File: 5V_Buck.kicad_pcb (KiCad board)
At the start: 2 copper layers, 34 x 40 mm, 12 parts, among them J1 POWER_JACK1, M1 USB+SHIELDUSB-A-S-NOSILK-FEMA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, U1 ADP2303ARDZ-5.0

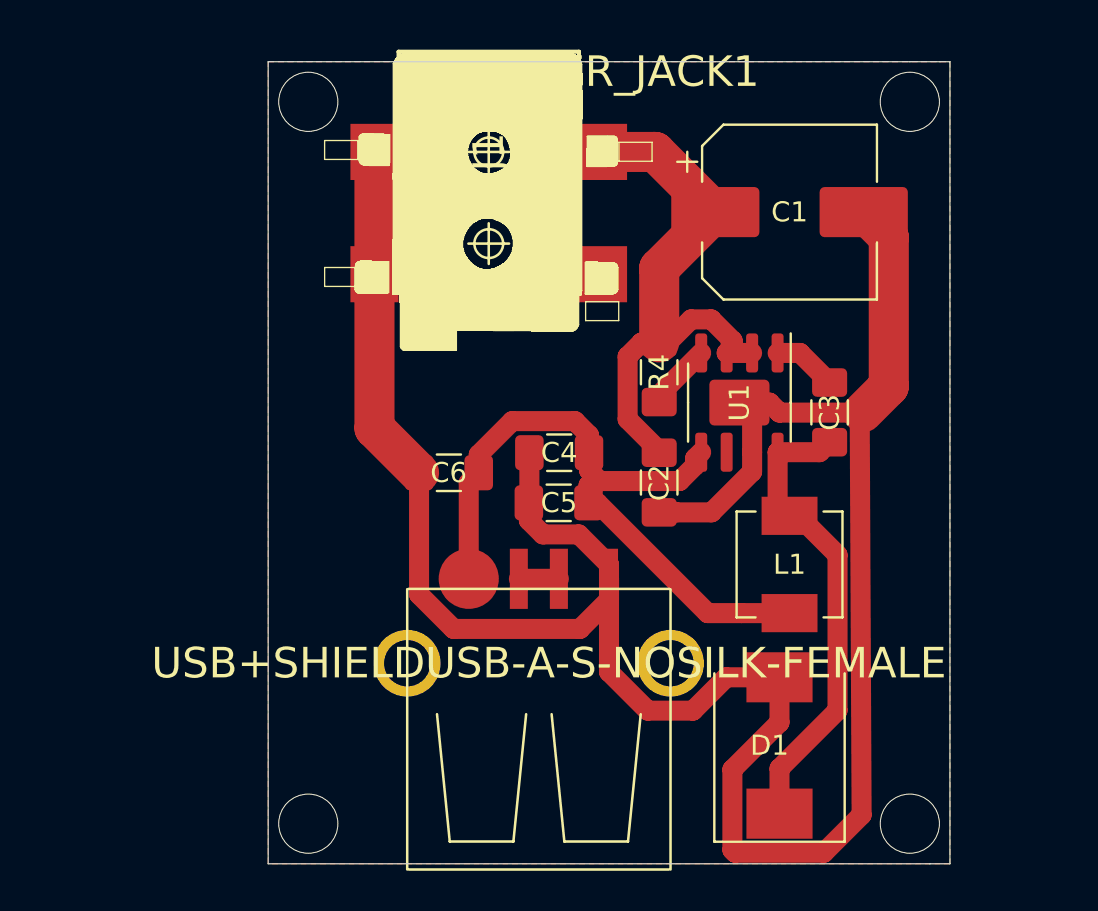
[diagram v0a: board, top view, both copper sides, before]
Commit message: Updating 3D view
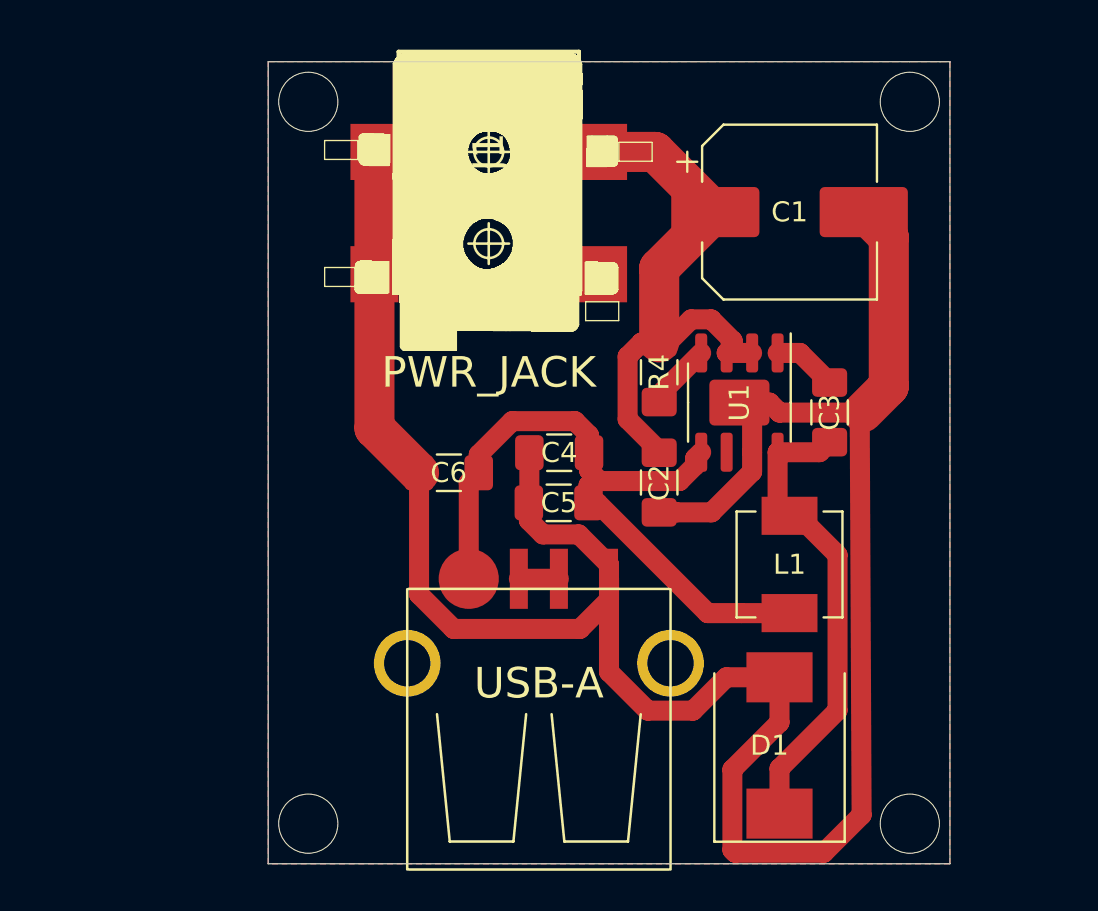
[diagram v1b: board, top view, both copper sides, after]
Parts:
- J1: value POWER_JACK1 -> PWR_JACK
- M1: value USB+SHIELDUSB-A-S-NOSILK-FEMALE -> USB-A
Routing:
- net (no net): vias 4 -> 6

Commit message: Creating a 3D box
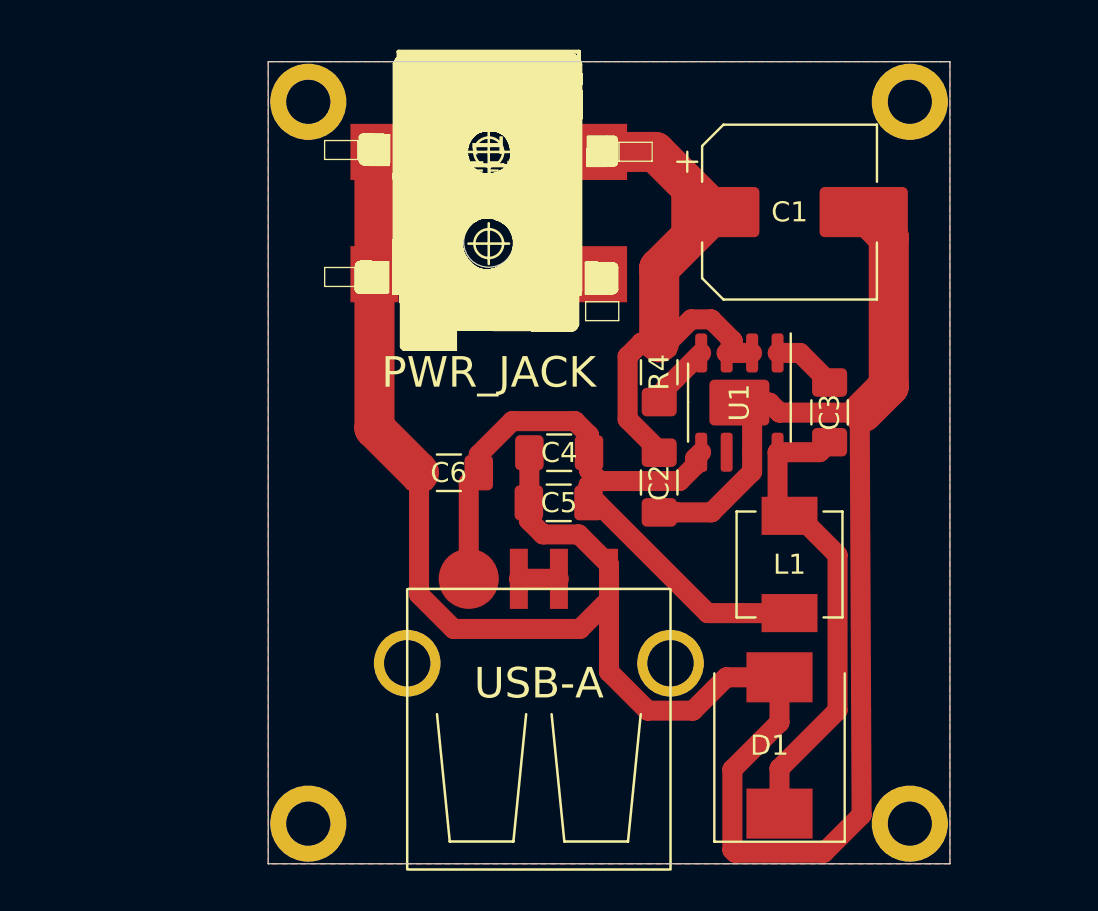
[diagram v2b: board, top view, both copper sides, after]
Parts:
- added REF**: MountingHole_2.5mm, MountingHole:MountingHole_2.5mm, F.Cu at (146.0, 76.5)
- added REF**: MountingHole_2.5mm, MountingHole:MountingHole_2.5mm, F.Cu at (146.0, 72.0)
- added REF**: MountingHole_2.2mm_M2_DIN965_Pad, MountingHole:MountingHole_2.2mm_M2_DIN965_Pad, F.Cu at (137.0, 105.5)
- added REF**: MountingHole_2.2mm_M2_DIN965_Pad, MountingHole:MountingHole_2.2mm_M2_DIN965_Pad, F.Cu at (167.0, 105.5)
- added REF**: MountingHole_2.2mm_M2_DIN965_Pad, MountingHole:MountingHole_2.2mm_M2_DIN965_Pad, F.Cu at (167.0, 69.5)
- added REF**: MountingHole_2.2mm_M2_DIN965_Pad, MountingHole:MountingHole_2.2mm_M2_DIN965_Pad, F.Cu at (137.0, 69.5)
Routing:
- net (no net): vias 6 -> 0
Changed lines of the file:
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@@
   (general
     (thickness 1.6)
-    (drawings 12)
-    (tracks 97)
+    (drawings 11)
+    (tracks 91)
     (zones 0)
-    (modules 12)
+    (modules 18)
     (nets 7)
   )
@@
     (add_net "Net-(R4-Pad1)")
   )
+  (module MountingHole:MountingHole_2.5mm (layer F.Cu)
+    (at 146 76.5)
+    (descr "Mounting Hole 2.5mm, no annular")
+    (tags "mounting hole 2.5mm no annular")
+    (attr virtual)
+    (fp_text reference REF** (at 0 -3.5) (layer F.SilkS)
+      (effects (font (size 1 1) (thickness 0.15)))
+    )
+    (fp_text value MountingHole_2.5mm (at 0 3.5) (layer F.Fab)
+      (effects (font (size 1 1) (thickness 0.15)))
+    )
+    (fp_text user %R (at 0.3 0) (layer F.Fab)
+      (effects (font (size 1 1) (thickness 0.15)))
+    )
+    (fp_circle (center 0 0) (end 2.5 0) (layer Cmts.User) (width 0.15))
+    (fp_circle (center 0 0) (end 2.75 0) (layer F.CrtYd) (width 0.05))
+    (pad 1 np_thru_hole circle (at 0 0) (size 2.5 2.5) (drill 2.5) (layers *.Cu *.Mask))
+  )
+  (module MountingHole:MountingHole_2.5mm (layer F.Cu)
+    (at 146 72)
+    (descr "Mounting Hole 2.5mm, no annular")
+    (tags "mounting hole 2.5mm no annular")
+    (attr virtual)
+    (fp_text reference REF** (at 0 -3.5) (layer F.SilkS)
+      (effects (font (size 1 1) (thickness 0.15)))
+    )
+    (fp_text value MountingHole_2.5mm (at 0 3.5) (layer F.Fab)
+      (effects (font (size 1 1) (thickness 0.15)))
+    )
+    (fp_circle (center 0 0) (end 2.75 0) (layer F.CrtYd) (width 0.05))
+    (fp_circle (center 0 0) (end 2.5 0) (layer Cmts.User) (width 0.15))
+    (fp_text user %R (at 0.3 0) (layer F.Fab)
+      (effects (font (size 1 1) (thickness 0.15)))
+    )
+    (pad 1 np_thru_hole circle (at 0 0) (size 2.5 2.5) (drill 2.5) (layers *.Cu *.Mask))
+  )
+  (module MountingHole:MountingHole_2.2mm_M2_DIN965_Pad (layer F.Cu)
+    (at 137 105.5)
+    (descr "Mounting Hole 2.2mm, M2, DIN965")
+    (tags "mounting hole 2.2mm m2 din965")
+    (attr virtual)
+    (fp_text reference REF** (at 0 -2.9) (layer F.SilkS) hide
+      (effects (font (size 1 1) (thickness 0.15)))
+    )
+    (fp_text value MountingHole_2.2mm_M2_DIN965_Pad (at 0 2.9) (layer F.Fab)
+      (effects (font (size 1 1) (thickness 0.15)))
+    )
+    (fp_text user %R (at 0.3 0) (layer F.Fab)
+      (effects (font (size 1 1) (thickness 0.15)))
+    )
+    (fp_circle (center 0 0) (end 1.9 0) (layer Cmts.User) (width 0.15))
+    (fp_circle (center 0 0) (end 2.15 0) (layer F.CrtYd) (width 0.05))
+    (pad 1 thru_hole circle (at 0 0) (size 3.8 3.8) (drill 2.2) (layers *.Cu *.Mask))
+  )
+  (module MountingHole:MountingHole_2.2mm_M2_DIN965_Pad (layer F.Cu)
+    (at 167 105.5)
+    (descr "Mounting Hole 2.2mm, M2, DIN965")
+    (tags "mounting hole 2.2mm m2 din965")
+    (attr virtual)
+    (fp_text reference REF** (at 0 -2.9) (layer F.SilkS) hide
+      (effects (font (size 1 1) (thickness 0.15)))
+    )
+    (fp_text value MountingHole_2.2mm_M2_DIN965_Pad (at 0 2.9) (layer F.Fab)
+      (effects (font (size 1 1) (thickness 0.15)))
+    )
+    (fp_circle (center 0 0) (end 2.15 0) (layer F.CrtYd) (width 0.05))
+    (fp_circle (center 0 0) (end 1.9 0) (layer Cmts.User) (width 0.15))
+    (fp_text user %R (at 0.3 0) (layer F.Fab)
+      (effects (font (size 1 1) (thickness 0.15)))
+    )
+    (pad 1 thru_hole circle (at 0 0) (size 3.8 3.8) (drill 2.2) (layers *.Cu *.Mask))
+  )
+  (module MountingHole:MountingHole_2.2mm_M2_DIN965_Pad (layer F.Cu)
+    (at 167 69.5)
+    (descr "Mounting Hole 2.2mm, M2, DIN965")
+    (tags "mounting hole 2.2mm m2 din965")
+    (attr virtual)
+    (fp_text reference REF** (at 0 -2.9) (layer F.SilkS) hide
+      (effects (font (size 1 1) (thickness 0.15)))
+    )
+    (fp_text value MountingHole_2.2mm_M2_DIN965_Pad (at 0 2.9) (layer F.Fab)
+      (effects (font (size 1 1) (thickness 0.15)))
+    )
+    (fp_text user %R (at 0.3 0) (layer F.Fab)
+      (effects (font (size 1 1) (thickness 0.15)))
+    )
+    (fp_circle (center 0 0) (end 1.9 0) (layer Cmts.User) (width 0.15))
+    (fp_circle (center 0 0) (end 2.15 0) (layer F.CrtYd) (width 0.05))
+    (pad 1 thru_hole circle (at 0 0) (size 3.8 3.8) (drill 2.2) (layers *.Cu *.Mask))
+  )
+  (module MountingHole:MountingHole_2.2mm_M2_DIN965_Pad (layer F.Cu)
+    (at 137 69.5)
+    (descr "Mounting Hole 2.2mm, M2, DIN965")
+    (tags "mounting hole 2.2mm m2 din965")
+    (attr virtual)
+    (fp_text reference REF** (at 0 3.5) (layer F.SilkS) hide
+      (effects (font (size 1 1) (thickness 0.15)))
+    )
+    (fp_text value MountingHole_2.2mm_M2_DIN965_Pad (at 0 2.9) (layer F.Fab)
+      (effects (font (size 1 1) (thickness 0.15)))
+    )
+    (fp_circle (center 0 0) (end 2.15 0) (layer F.CrtYd) (width 0.05))
+    (fp_circle (center 0 0) (end 1.9 0) (layer Cmts.User) (width 0.15))
+    (fp_text user %R (at 0.3 0) (layer F.Fab)
+      (effects (font (size 1 1) (thickness 0.15)))
+    )
+    (pad 1 thru_hole circle (at 0 0) (size 3.8 3.8) (drill 2.2) (layers *.Cu *.Mask))
+  )
   (module SparkFun-Connectors:POWER_JACK_SMD_OVERPASTE_REDBOARD_0603 (layer F.Cu)
     (at 146 72 270)
@@
     (pad 2 smd rect (at 2.4265 0 270) (size 1.903 2.79) (layers F.Cu F.Paste F.Mask)
       (net 5 5V))
-    (model ${KISYS3DMOD}/Inductor_SMD.3dshapes/L_Vishay_IHLP-2020.wrl
-      (at (xyz 0 0 0))
+    (model ${KIPRJMOD}/3D/ihlp2020bzer6r8m01.stp
+      (offset (xyz -0.75 6 -2.5))
       (scale (xyz 1 1 1))
-      (rotate (xyz 0 0 0))
+      (rotate (xyz -90 0 0))
     )
   )
@@
     (pad 8 smd roundrect (at 2.475 -1.905 270) (size 1.95 0.6) (layers F.Cu F.Paste F.Mask) (roundrect_rratio 0.25)
       (net 2 "Net-(C3-Pad2)"))
-    (model ${KISYS3DMOD}/Package_SO.3dshapes/SOIC-8-1EP_3.9x4.9mm_P1.27mm_EP2.29x3mm.wrl
-      (at (xyz 0 0 0))
-      (scale (xyz 1 1 1))
-      (rotate (xyz 0 0 0))
-    )
     (model ${KIPRJMOD}/3D/SOIC-8_Package.step
       (at (xyz 0 0 0))
@@
     )
   )
-  (dimension 3 (width 0.15) (layer Eco2.User)
-    (gr_text "3,000 mm" (at 167 114.8) (layer Eco2.User)
-      (effects (font (size 1 1) (thickness 0.15)))
-    )
-    (feature1 (pts (xy 168.5 105.5) (xy 168.5 114.086421)))
-    (feature2 (pts (xy 165.5 105.5) (xy 165.5 114.086421)))
-    (crossbar (pts (xy 165.5 113.5) (xy 168.5 113.5)))
-    (arrow1a (pts (xy 168.5 113.5) (xy 167.373496 114.086421)))
-    (arrow1b (pts (xy 168.5 113.5) (xy 167.373496 112.913579)))
-    (arrow2a (pts (xy 165.5 113.5) (xy 166.626504 114.086421)))
-    (arrow2b (pts (xy 165.5 113.5) (xy 166.626504 112.913579)))
-  )
   (dimension 36 (width 0.15) (layer Eco2.User)
     (gr_text "36,000 mm" (at 128.7 87.5 270) (layer Eco2.User)
@@
   (gr_line (start 135 107.5) (end 168 107.5) (layer Edge.Cuts) (width 0.05))
   (segment (start 147.50178 93.28868) (end 149.49822 93.28868) (width 1) (layer F.Cu) (net 0))
-  (via (at 167 69.5) (size 3) (drill 2.9) (layers F.Cu B.Cu) (net 0))
-  (via (at 137 69.5) (size 3) (drill 2.9) (layers F.Cu B.Cu) (net 0))
-  (via (at 167 105.5) (size 3) (drill 2.9) (layers F.Cu B.Cu) (net 0))
-  (via (at 137 105.5) (size 3) (drill 2.9) (layers F.Cu B.Cu) (net 0))
-  (via (at 146 72) (size 3) (drill 2.9) (layers F.Cu B.Cu) (net 0))
-  (via (at 146 76.5) (size 3) (drill 2.9) (layers F.Cu B.Cu) (net 0))
   (segment (start 159.135 85.135) (end 158.5 84.5) (width 1) (layer F.Cu) (net 1) (status 30))
   (segment (start 159.135 86.975) (end 159.135 85.135) (width 1) (layer F.Cu) (net 1) (status 30))
@@
     (connect_pads (clearance 0.508))
     (min_thickness 0.254)
-    (fill (arc_segments 32) (thermal_gap 0.508) (thermal_bridge_width 0.508))
+    (fill yes (arc_segments 32) (thermal_gap 0.508) (thermal_bridge_width 0.508))
     (polygon
       (pts
